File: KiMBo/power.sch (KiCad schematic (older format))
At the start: 33 parts

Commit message: Bring more interfaces out to the root sheet and begin connecting modules
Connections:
- net SYS_RESET# renamed ~SYS_RESET

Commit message: Create nodes for more SS, add H stepper, begin fixing power rail names
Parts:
- added C? (x5): 100nF, symbol C
- added FB? (x5): FILTER, symbol FILTER
- added FL?: CM CHOKE, symbol EMI_FILTER_4pin
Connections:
- net labels added: +1.8VADC, +1V8, AVCC, VCC1, VCC2, VCC3, VCC4
- wire segments 225 -> 388

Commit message: Update the rest of the power rails and add two more stepper drivers
Now has *nine* stepper drivers, this will increase cost, and may drastically increase development time...
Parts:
- R?: value R -> 100mΩ
- SW?: value SW_DPST_Small -> RESET
- SW?: value SW_DPST_Small -> POWER
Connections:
- net labels added: CGND, SYS_5V, USB_DC, VDD_1V8, VDD_3V3A, VDD_3V3AUX, VDD_3V3B, VDD_5V, VDD_ADC, VDD_CORE, VDD_DDR, VDD_MPU, VDD_PLL, VDD_RTC
- net labels removed: +1.8VADC, +1V8
- wire segments 388 -> 264
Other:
- note added: "Internal Power Supply\nTest Point"
- note added: "Output Power Supply\nSecondary, 3.3VDC"
- note added: "TPS65217C\nOutput"
- moved on the sheet: D?, R?

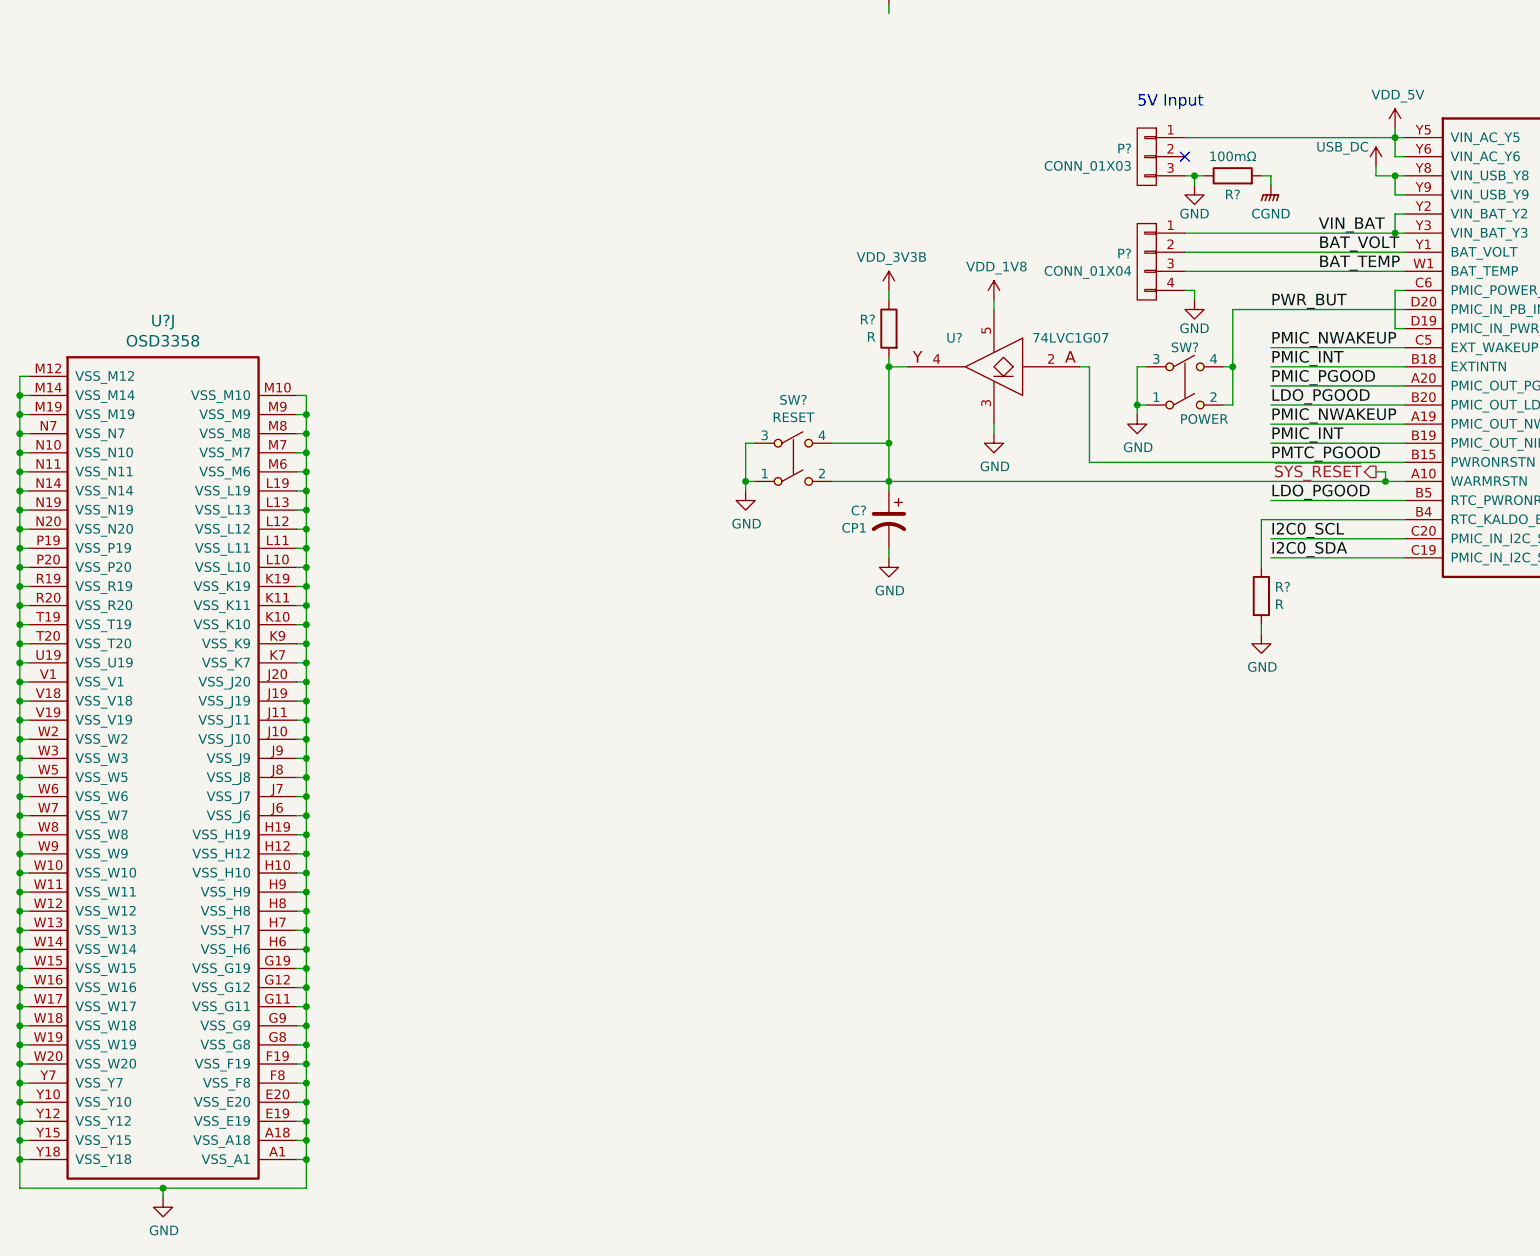
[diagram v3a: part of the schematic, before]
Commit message: Use only one driver on Y, NAND X and Z FAULT and SG signals
Dual X carriage will need to be tested to determine if two seperate drivers are required for X
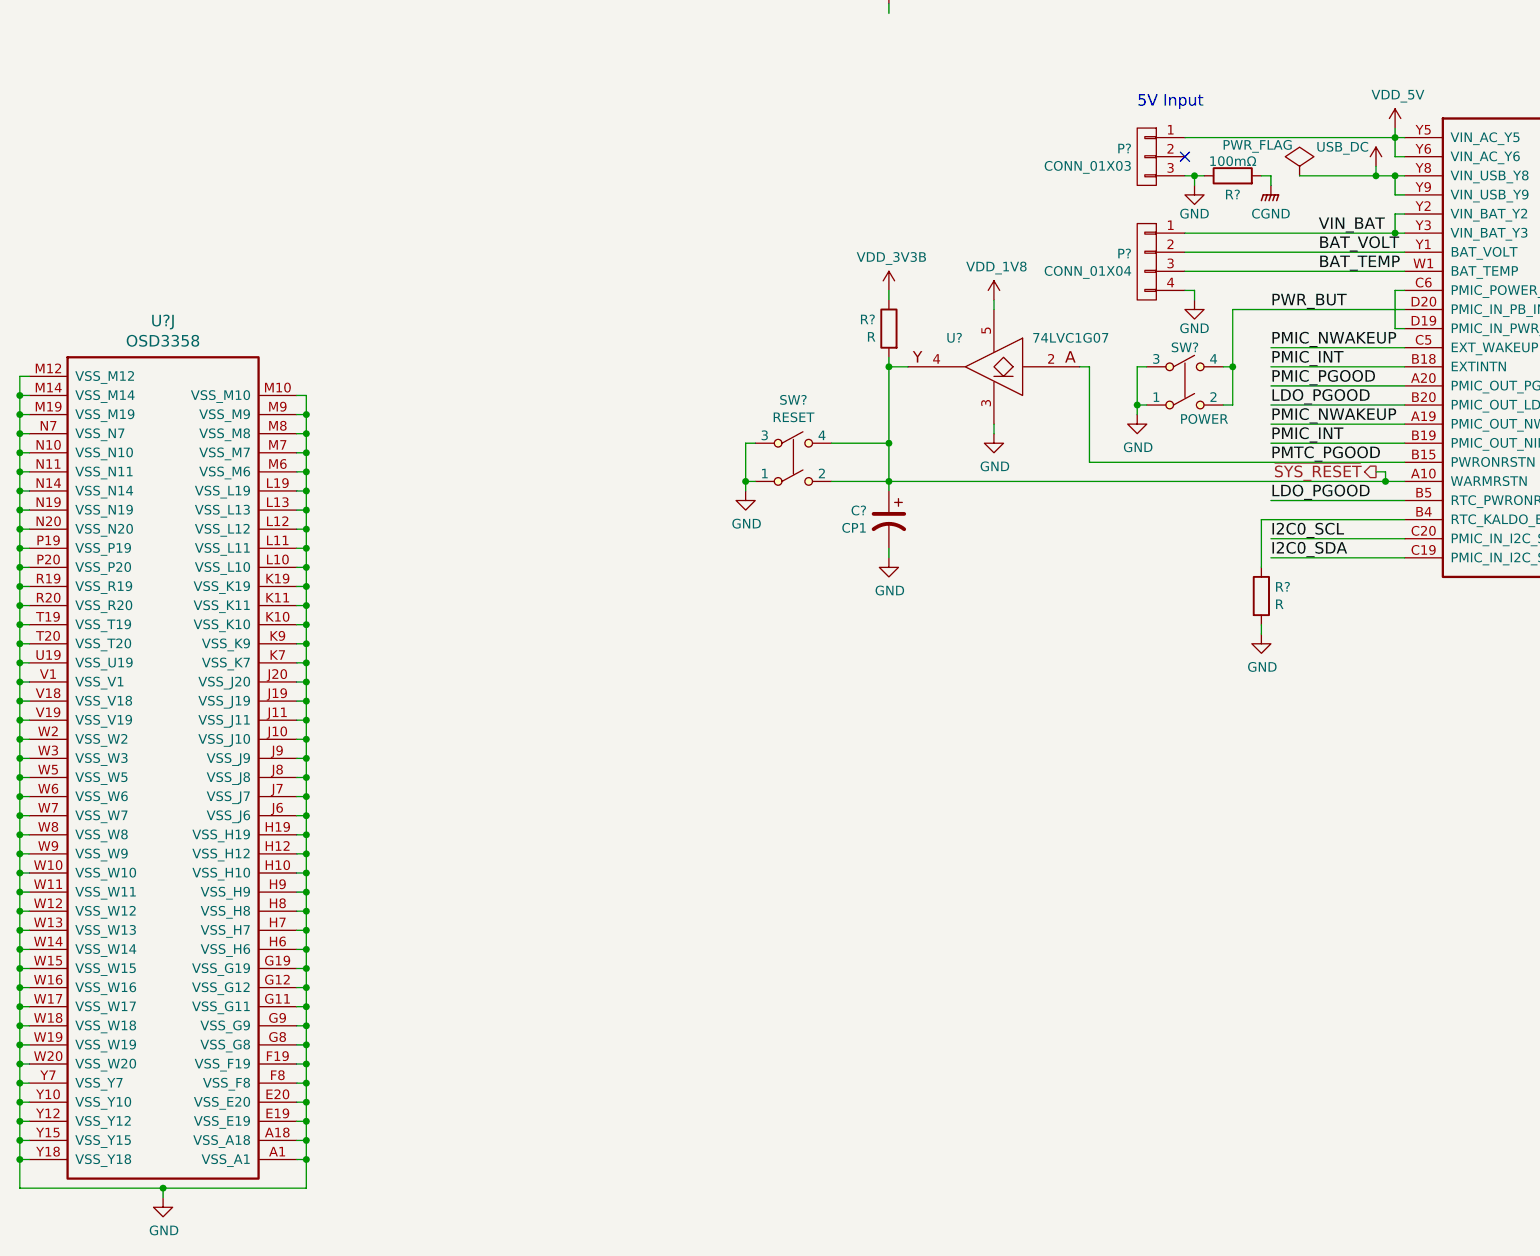
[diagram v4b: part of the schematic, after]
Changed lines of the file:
@@
 $Descr A3 16535 11693
 encoding utf-8
-Sheet 2 27
+Sheet 2 26
 Title ""
 Date ""
@@
 P 7500 5200
 F 0 "R?" V 7400 5200 50  0000 C CNN
-F 1 "100mΩ" V 7600 5200 50  0000 C CNN
+F 1 "100mΩ" V 7575 5200 50  0000 C CNN
 F 2 "" V 7430 5200 50  0000 C CNN
 F 3 "" H 7500 5200 50  0000 C CNN
@@
 	2600 6350 2650 6350
 Wire Wire Line
-	2650 6350 2650 10500
+	2650 10500 2650 6350
 Wire Wire Line
 	2650 10350 2600 10350
@@
 Connection ~ 2650 10250
 Wire Wire Line
-	2650 10500 1150 10500
+	1150 10500 2650 10500
 Connection ~ 2650 10350
 Connection ~ 1150 10350
@@
 	8350 5300 8350 5200
 Wire Wire Line
-	8250 5200 8400 5200
+	7850 5200 8400 5200
 Wire Wire Line
 	8250 5200 8250 5150
@@
 Text Notes 10900 7400 0    60   ~ 0
 TPS65217C\nOutput
+$Comp
+L PWR_FLAG #FLG?
+U 1 1 5A9BB809
+P 7850 5200
+F 0 "#FLG?" H 7850 5295 50  0001 C CNN
+F 1 "PWR_FLAG" H 7630 5360 50  0000 C CNN
+F 2 "" H 7850 5200 50  0000 C CNN
+F 3 "" H 7850 5200 50  0000 C CNN
+	1    7850 5200
+	1    0    0    -1
+$EndComp
+Connection ~ 8250 5200
 $EndSCHEMATC

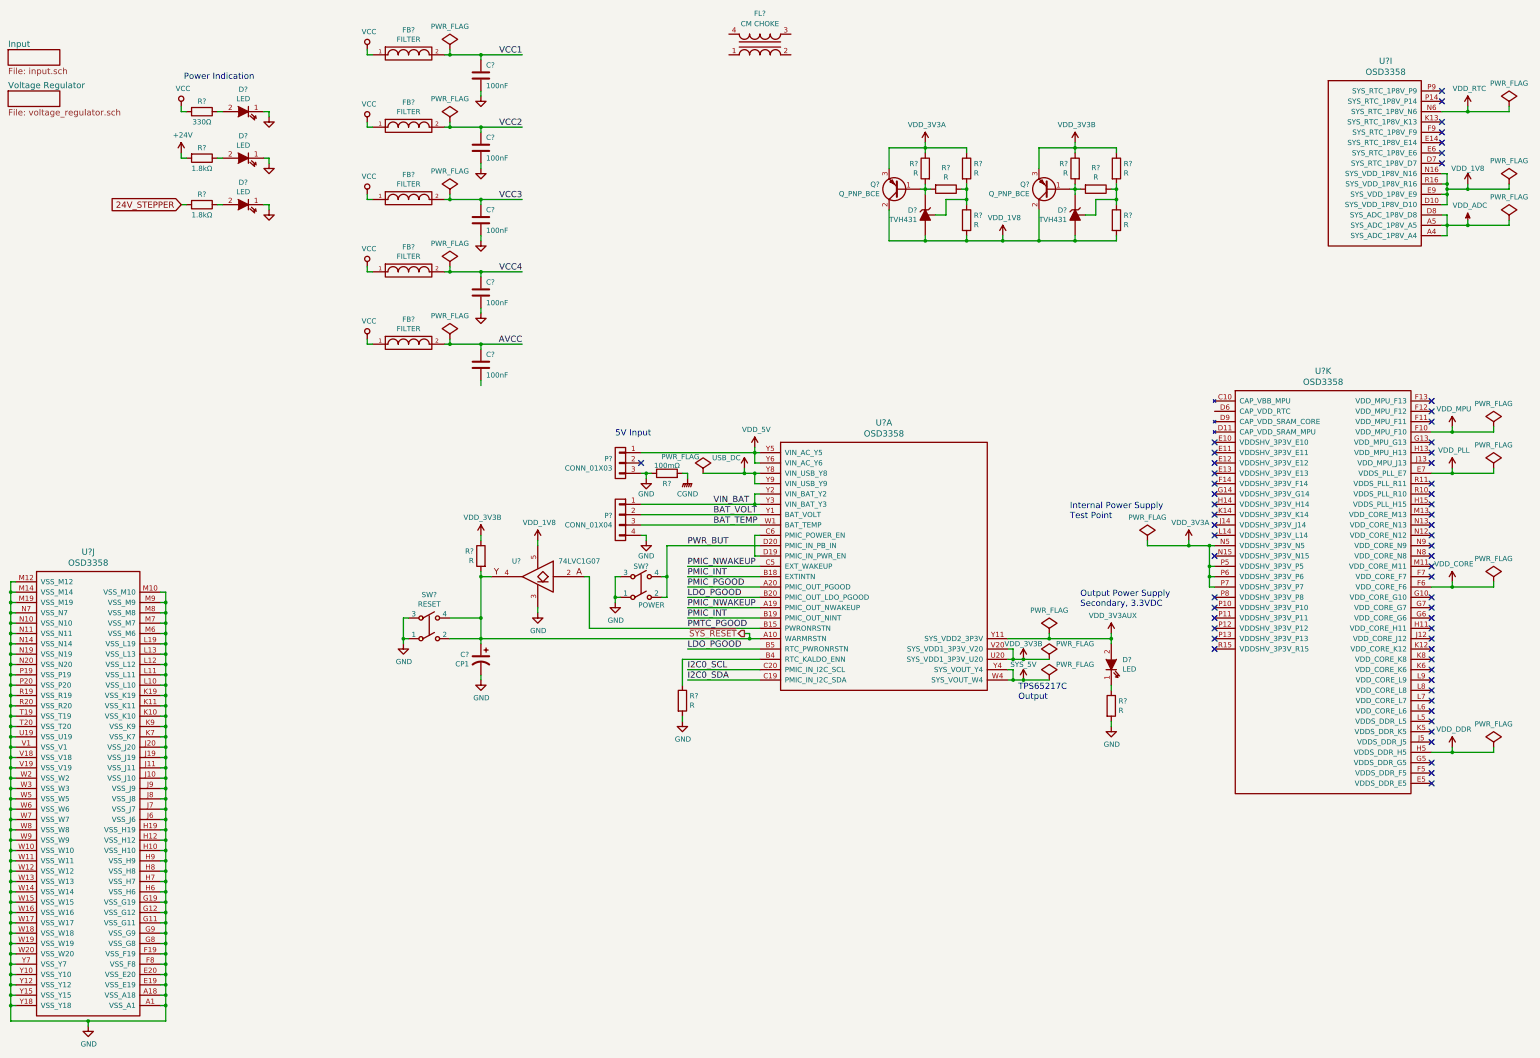
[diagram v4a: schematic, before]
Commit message: Show which components are DNP, begin spec of components, and refine the power input circuit
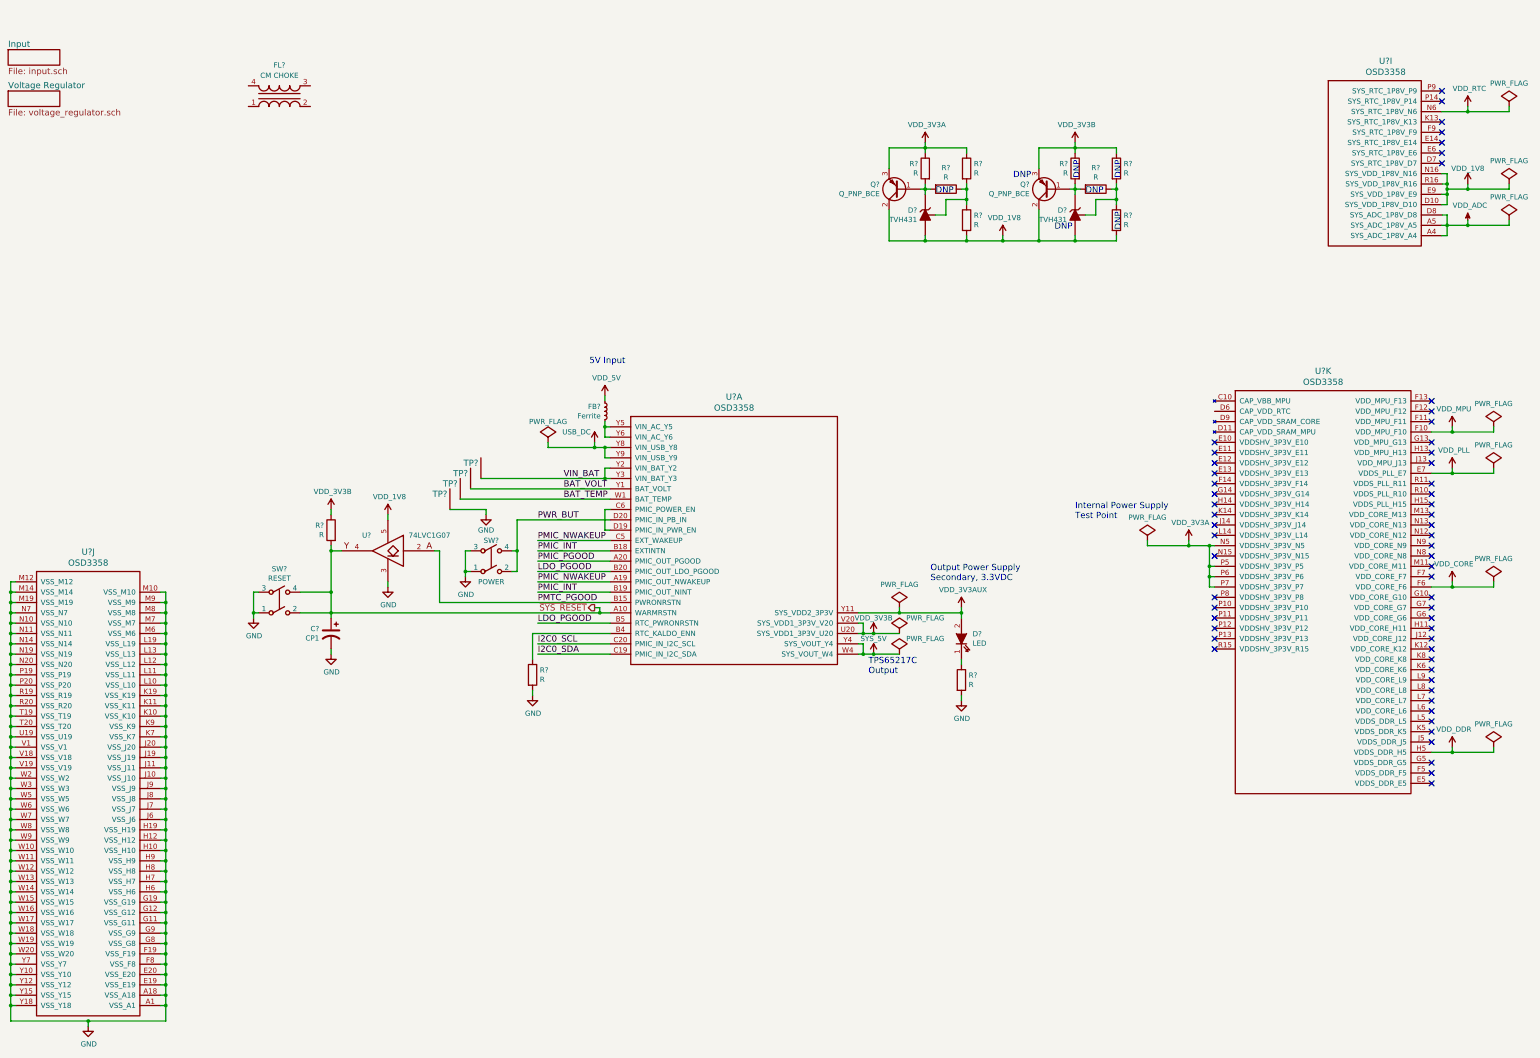
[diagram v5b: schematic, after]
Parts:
- removed C? (x5): 100nF, symbol C
- removed D? (x3): LED, symbol LED
- removed FB? (x5): FILTER, symbol FILTER
- removed P?: CONN_01X03, symbol CONN_01X03
- removed P?: CONN_01X04, symbol CONN_01X04
- removed R?: 330Ω, symbol R
- removed R? (x2): 1.8kΩ, symbol R
- removed R?: 100mΩ, symbol R
- added FB?: Ferrite, symbol INDUCTOR_Small
- added TP? (x4): TP, symbol TP
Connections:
- net BAT_TEMP: now also TP?.~
- net BAT_VOLT: now also TP?.~
- net GND: now also TP?.~
- net VDD_5V: now also FB?.2; no longer U?.Y5 (VIN_AC_Y5), U?.Y6 (VIN_AC_Y6)
- net VIN_BAT: now also TP?.~
- new net: FB?.1, U?.Y5 (VIN_AC_Y5), U?.Y6 (VIN_AC_Y6)
- no-connect marks 59 -> 58
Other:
- note added: "DNP"
- note removed: "Power Indication"
- moved on the sheet: C?, D?, FL?, R?, SW?, U?, U?A

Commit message: Add low pass filters to the outputs going to the heaters, fans, and to the endstop inputs.
The values of the passives need to be tweaked.
Ferrites need to be placed in series with the output to the heaters and fans.
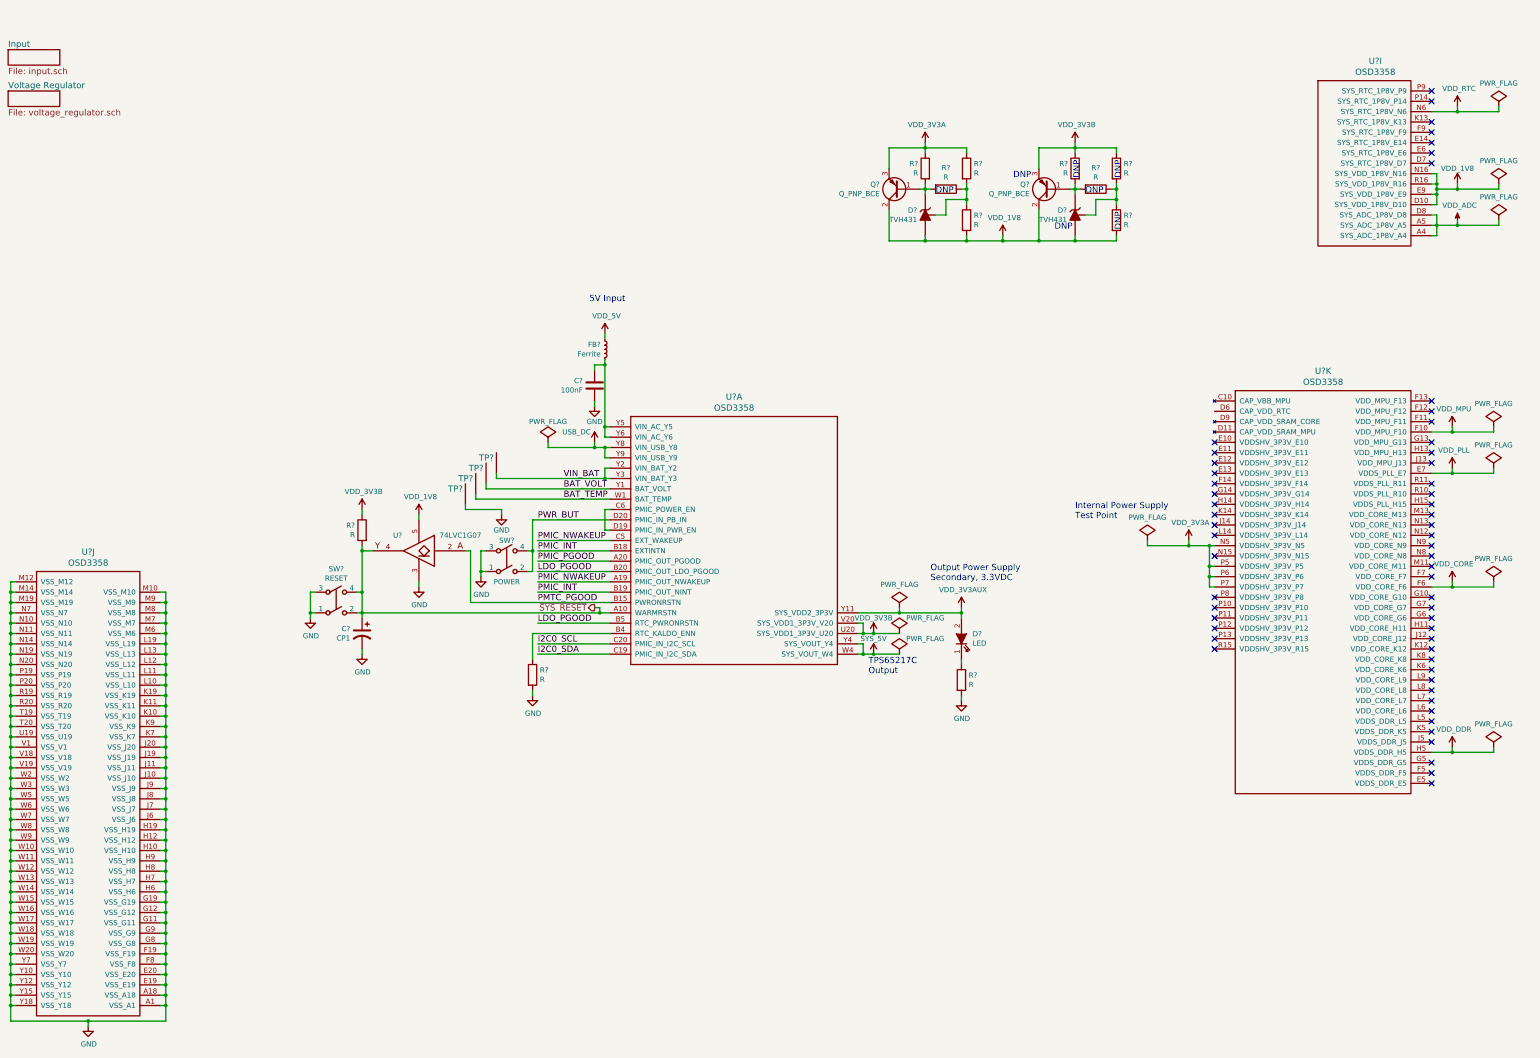
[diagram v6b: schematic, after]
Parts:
- removed FL?: CM CHOKE, symbol EMI_FILTER_4pin
- added C?: 100nF, symbol C
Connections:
- net GND: now also C?.2
- net at FB?.1, U?.Y5 (VIN_AC_Y5), U?.Y6 (VIN_AC_Y6): now also C?.1
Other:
- moved on the sheet: C?, FB?, R?, SW?, TP?, U?, U?I
